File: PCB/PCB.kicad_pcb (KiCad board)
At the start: 4 copper layers, 104.1 x 104.1 mm, 113 parts, among them J1 Conn_01x06_Female, J3 DB25_Receptacle_MountingHoles, U1 Hx711, U10 Hx711, U11 Hx711, U12 Hx711, U13 74HC165, U15 LT3042xMSE, U16 74HC165, U2 Hx711, U3 Hx711, U4 Hx711, U5 Hx711, U6 Hx711, U7 Hx711, U8 Hx711, U9 Hx711

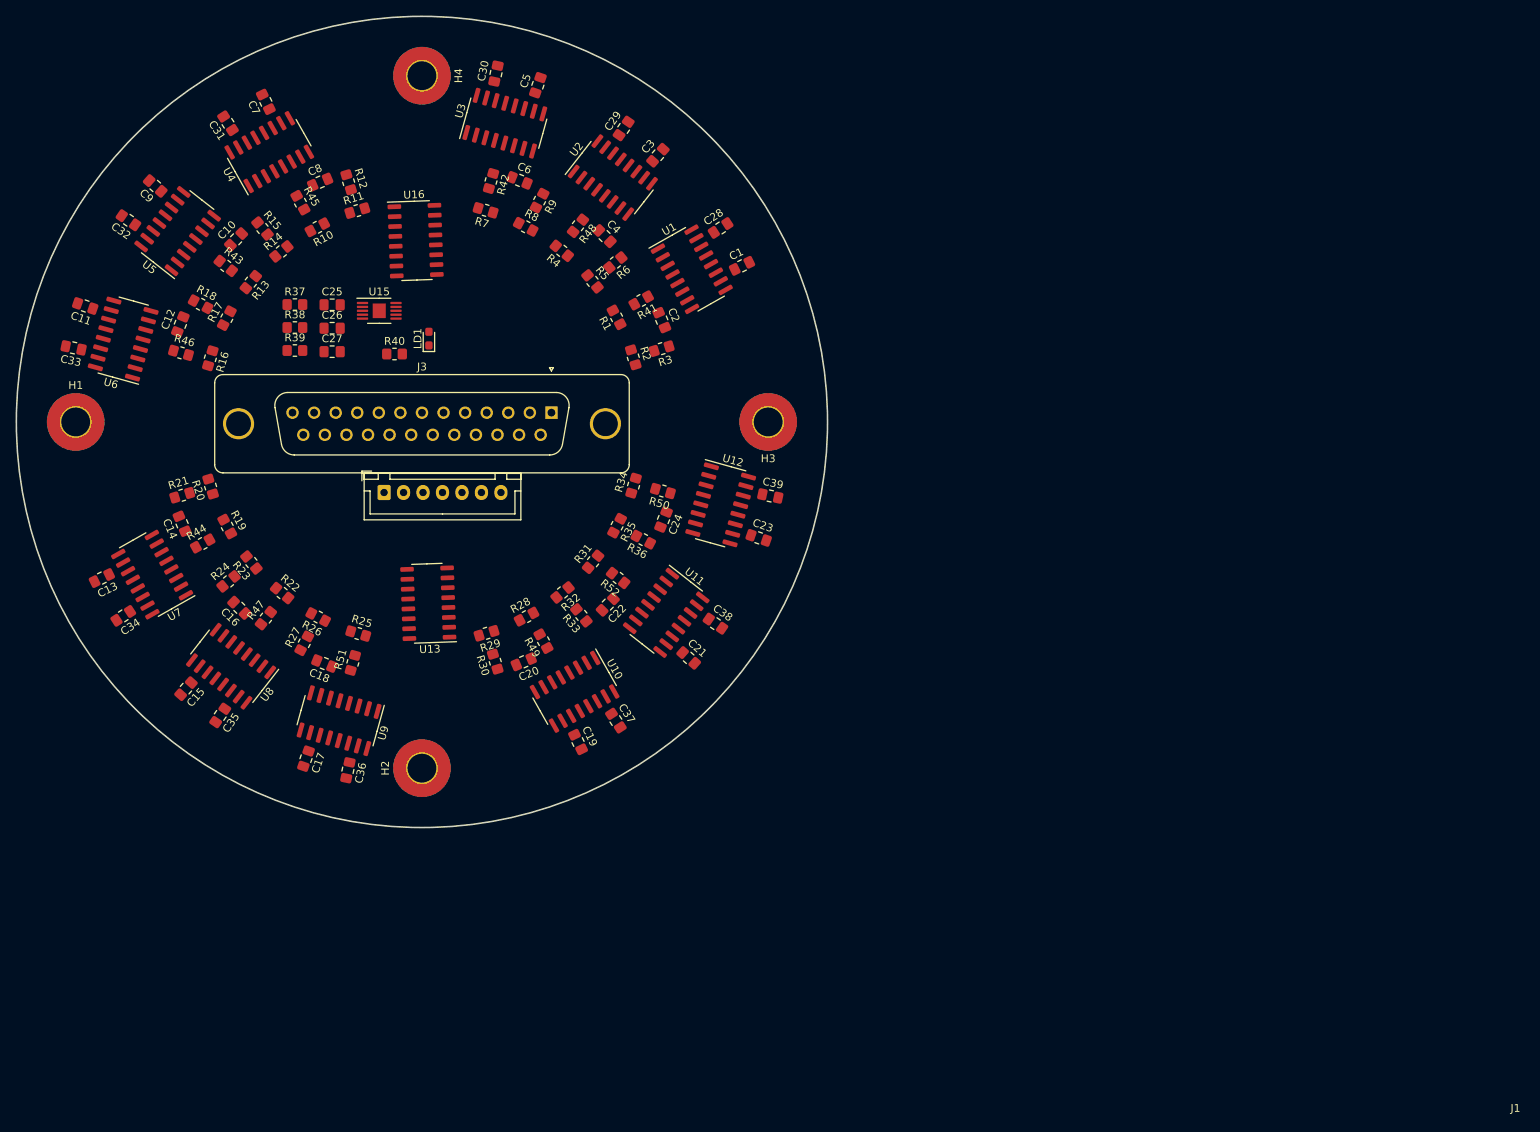
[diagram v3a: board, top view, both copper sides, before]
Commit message: Created outline and updated pcb
Started work on tracing the pcb now that I have a complete layout with a wiring channel cut out. Two planes have been laid out
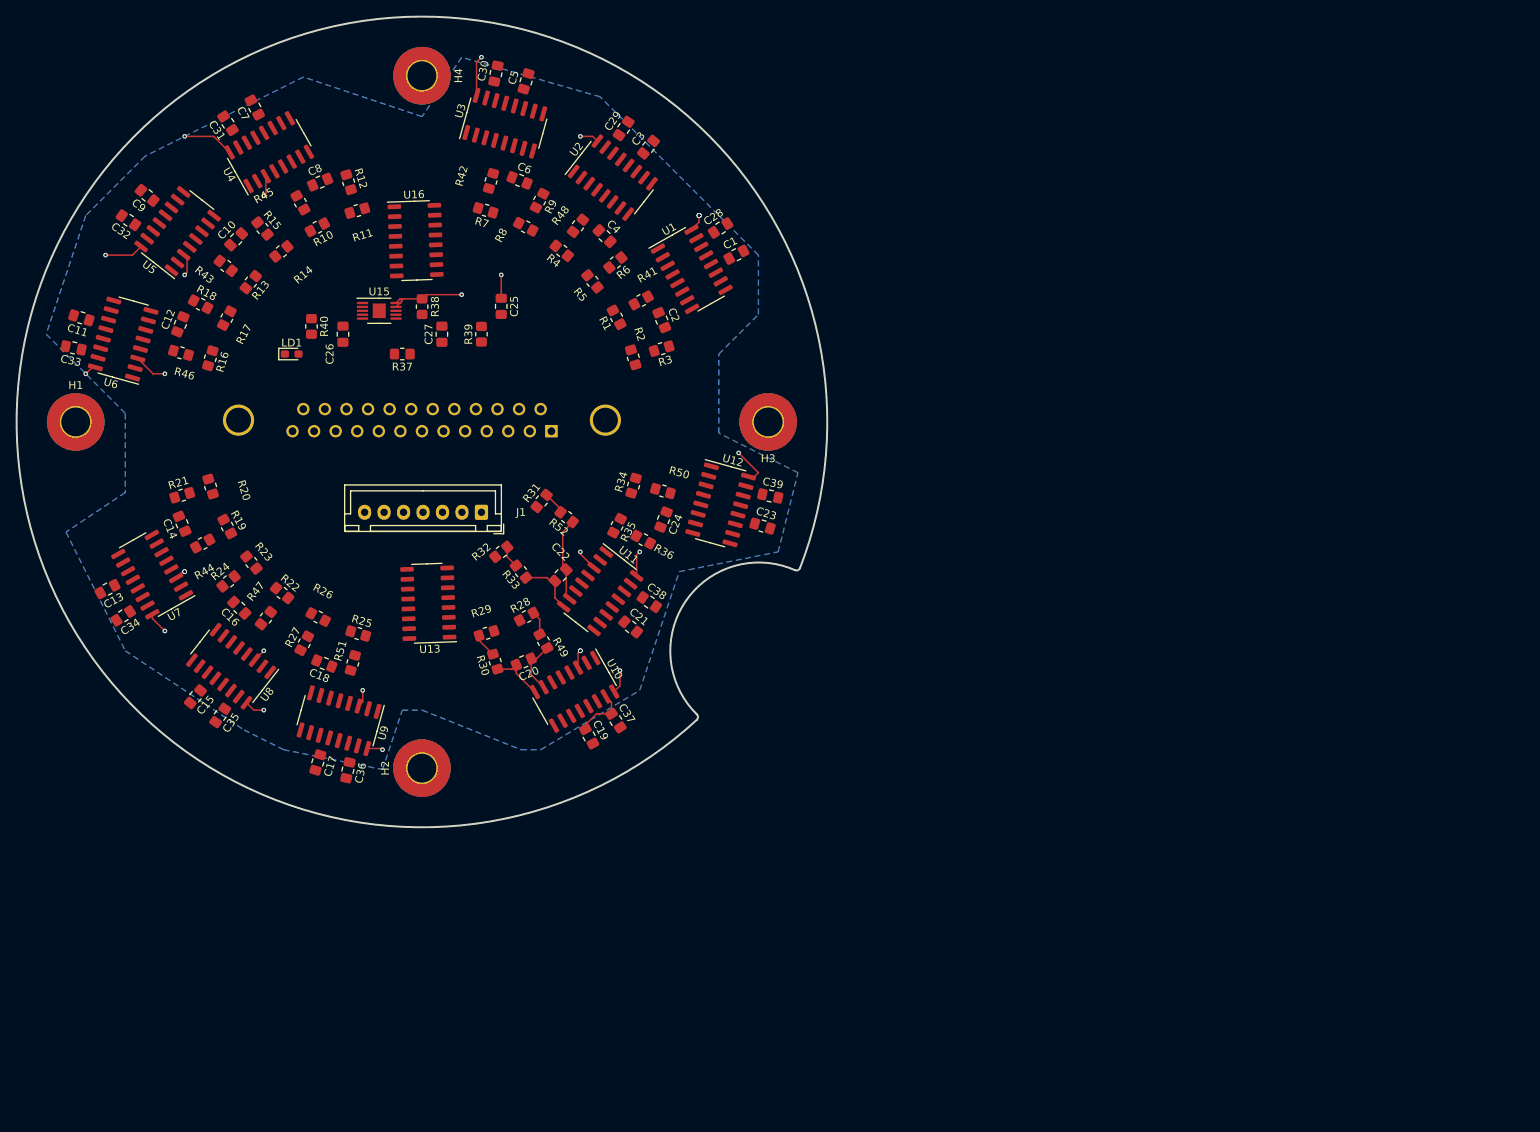
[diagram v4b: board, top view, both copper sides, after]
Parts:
- J3: moved to B.Cu
- moved R39 24.0 mm to (167.6, 78.7), turned to 90 degrees
- moved C25 21.7 mm to (170.2, 75.2), turned to -90 degrees
- moved LD1 17.7 mm to (143.3, 81.3), turned to 0 degrees
- moved R38 16.5 mm to (160.0, 75.2), turned to -90 degrees
- moved R37 15.2 mm to (157.5, 81.3), turned to 180 degrees
- moved C27 14.3 mm to (162.6, 78.7), turned to 90 degrees
- moved J1 12.8 mm to (167.6, 101.6), turned to 180 degrees
- moved R40 11.2 mm to (145.8, 77.7), turned to -90 degrees
- moved R52 10.2 mm to (178.6, 102.2)
- moved R31 10.2 mm to (175.4, 100.1)
- moved R33 9.57 mm to (172.7, 109.2)
- moved R32 9.44 mm to (170.2, 106.7), turned to 39.5 degrees
- moved U11 8.92 mm to (182.9, 111.7)
- moved C38 8.92 mm to (189.2, 113.1)
- moved C21 8.44 mm to (186.8, 116.3), turned to -39.5 degrees
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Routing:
- net +3.3V: track 0.00 -> 392.6 mm, vias 0 -> 16
- net 4.5V: track 0.00 -> 56.2 mm, vias 0 -> 12
- net Net-(U11-INA-): track 0.00 -> 10.8 mm
- net Net-(U11-INA+): track 0.00 -> 7.65 mm
- net Net-(U10-INA+): track 0.00 -> 7.11 mm
- net +5V: track 0.00 -> 7.05 mm
- net Net-(U10-INA-): track 0.00 -> 6.95 mm
- net /H13N: track 0.00 -> 3.13 mm
- net /H13P: track 0.00 -> 3.09 mm
- net /H5P: track 0.00 -> 2.98 mm
- net /H5N: track 0.00 -> 2.87 mm
- added copper zone on B.Cu, net +5V
- added copper zone on In1.Cu, net 4.5V
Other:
- outline, holes or cut-outs redrawn

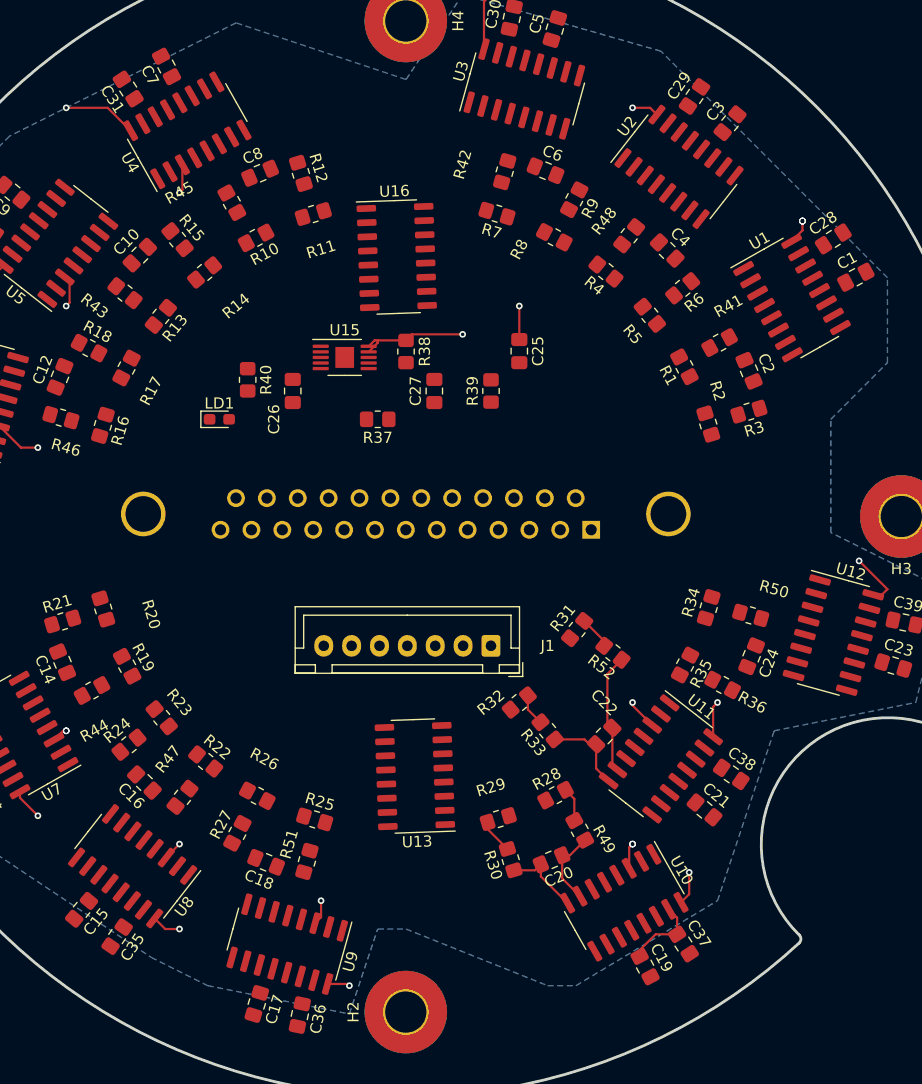
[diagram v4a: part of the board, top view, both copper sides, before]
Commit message: Updated pcb with tracing
2 more planes have been added and many wires are going around including clock lines
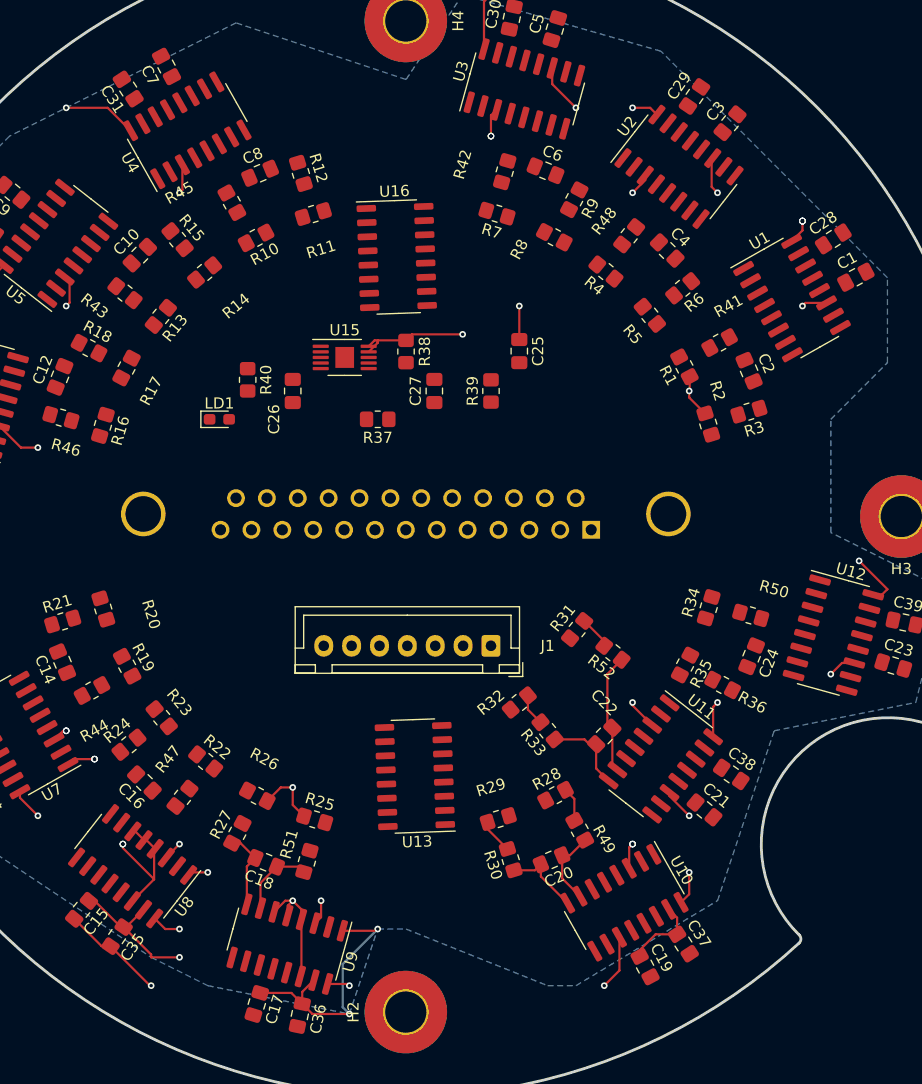
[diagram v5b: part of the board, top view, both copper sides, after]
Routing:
- net HX_CLK: track 0.00 -> 199.8 mm, vias 0 -> 6
- net GND: track 0.00 -> 54.1 mm, vias 0 -> 6
- net +5V: track 7.05 -> 48.1 mm, vias 0 -> 6
- net +3.3V: track 392.6 -> 375.3 mm
- net Net-(U9-INA+): track 0.00 -> 7.11 mm
- net Net-(U9-INA-): track 0.00 -> 6.95 mm
- net 4.5V: track 56.2 -> 60.8 mm, vias 12 -> 15
- added copper zone on In2.Cu, net GND

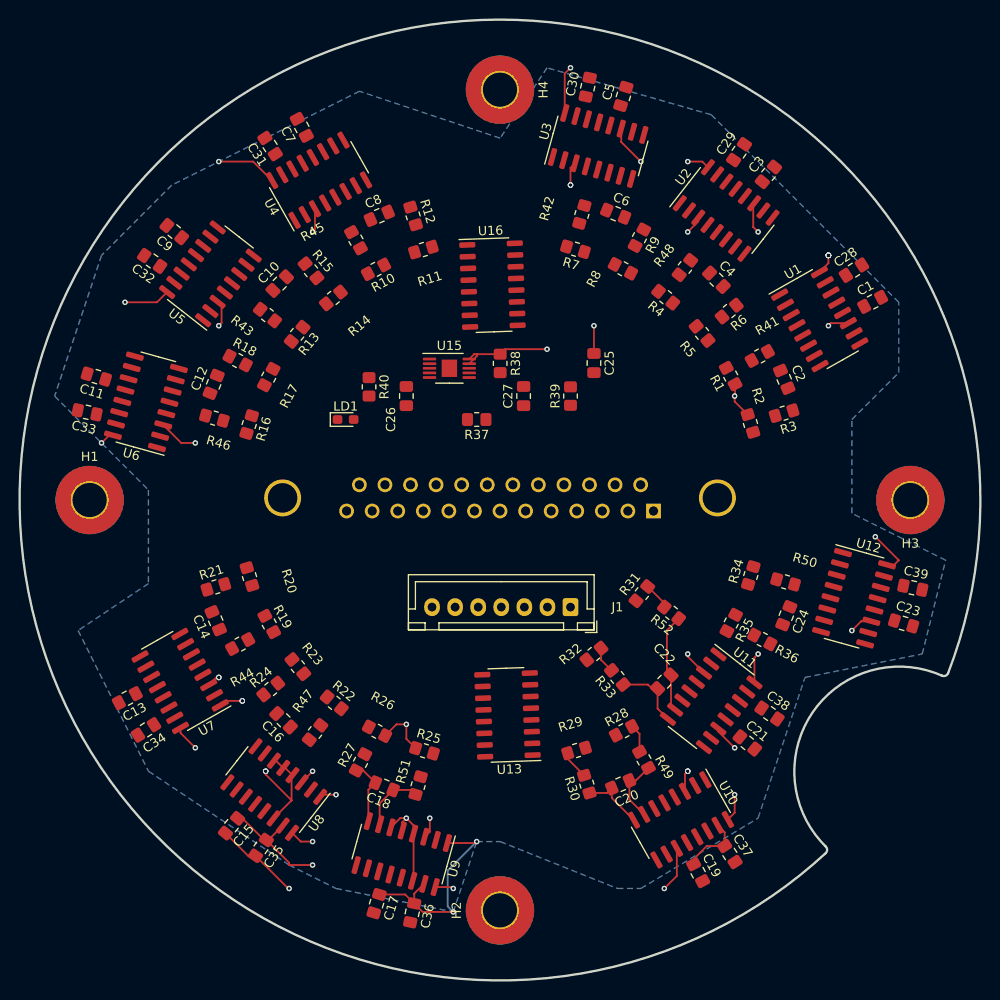
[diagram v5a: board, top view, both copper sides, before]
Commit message: Updated layout
Due to some complications during the first attempt at tracing, a new version of the board had to be created
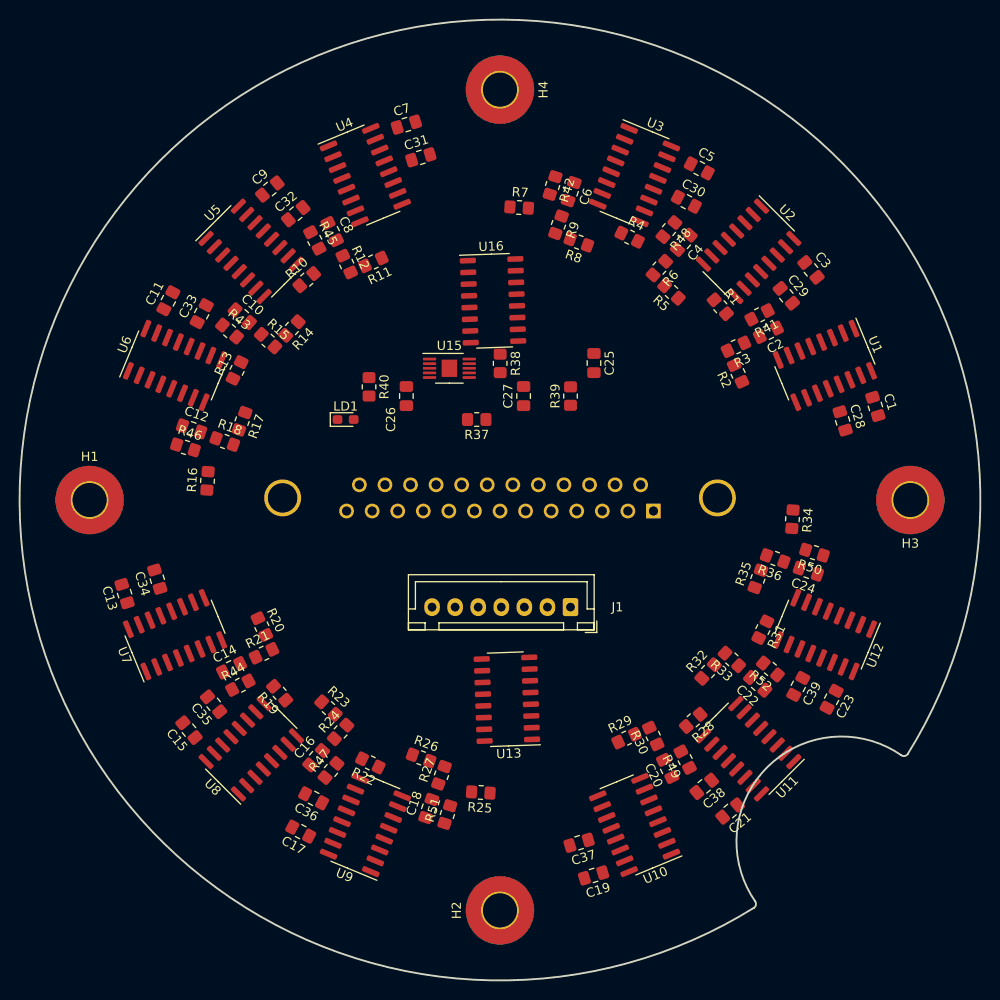
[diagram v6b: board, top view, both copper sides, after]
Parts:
- moved C35 16.4 mm to (129.0, 112.1), turned to 129.5 degrees
- moved C29 16.4 mm to (191.0, 67.9), turned to -50.5 degrees
- moved C32 16.4 mm to (137.9, 59.0), turned to 39.5 degrees
- moved C33 16.4 mm to (127.7, 69.8), turned to 62 degrees
- moved C36 16.4 mm to (139.8, 122.3), turned to 152 degrees
- moved C39 16.4 mm to (192.3, 110.2), turned to -118 degrees
- moved C30 16.4 mm to (180.2, 57.7), turned to -28 degrees
- moved C28 16.4 mm to (197.1, 81.4), turned to -73 degrees
- moved C34 16.4 mm to (122.9, 98.6), turned to 107 degrees
- moved C37 16.4 mm to (168.6, 127.1), turned to -163 degrees
- moved C31 16.4 mm to (151.4, 52.9), turned to 17 degrees
- moved R31 13.7 mm to (188.5, 104.0), turned to -116.25 degrees
- moved R33 12.6 mm to (185.1, 107.3), turned to 137.5 degrees
- moved R32 12.5 mm to (182.5, 108.6), turned to 47.5 degrees
- moved R52 12.3 mm to (189.3, 108.3), turned to 140 degrees
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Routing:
- net +3.3V: track 375.3 -> 0.00 mm, vias 16 -> 0
- net HX_CLK: track 199.8 -> 0.00 mm, vias 6 -> 0
- net 4.5V: track 60.8 -> 0.00 mm, vias 15 -> 0
- net GND: track 54.1 -> 0.00 mm, vias 6 -> 0
- net +5V: track 48.1 -> 0.00 mm, vias 6 -> 0
- net Net-(U11-INA-): track 10.8 -> 0.00 mm
- net Net-(U11-INA+): track 7.65 -> 0.00 mm
- net Net-(U9-INA+): track 7.11 -> 0.00 mm
- net Net-(U10-INA+): track 7.11 -> 0.00 mm
- net Net-(U9-INA-): track 6.95 -> 0.00 mm
- net Net-(U10-INA-): track 6.95 -> 0.00 mm
- net /H13N: track 3.13 -> 0.00 mm
- net /H13P: track 3.09 -> 0.00 mm
- net /H5P: track 2.98 -> 0.00 mm
- net /H5N: track 2.87 -> 0.00 mm
- removed copper zone on B.Cu, net +5V
- removed copper zone on In1.Cu, net 4.5V
- removed copper zone on In2.Cu, net GND
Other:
- outline, holes or cut-outs redrawn
